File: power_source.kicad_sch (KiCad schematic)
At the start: 16 parts, among them CN1 KF250-3.5-2P-2, Q1 PJM2309PSC, U1 AP63203WU, U2 B0303S-1W_C883455

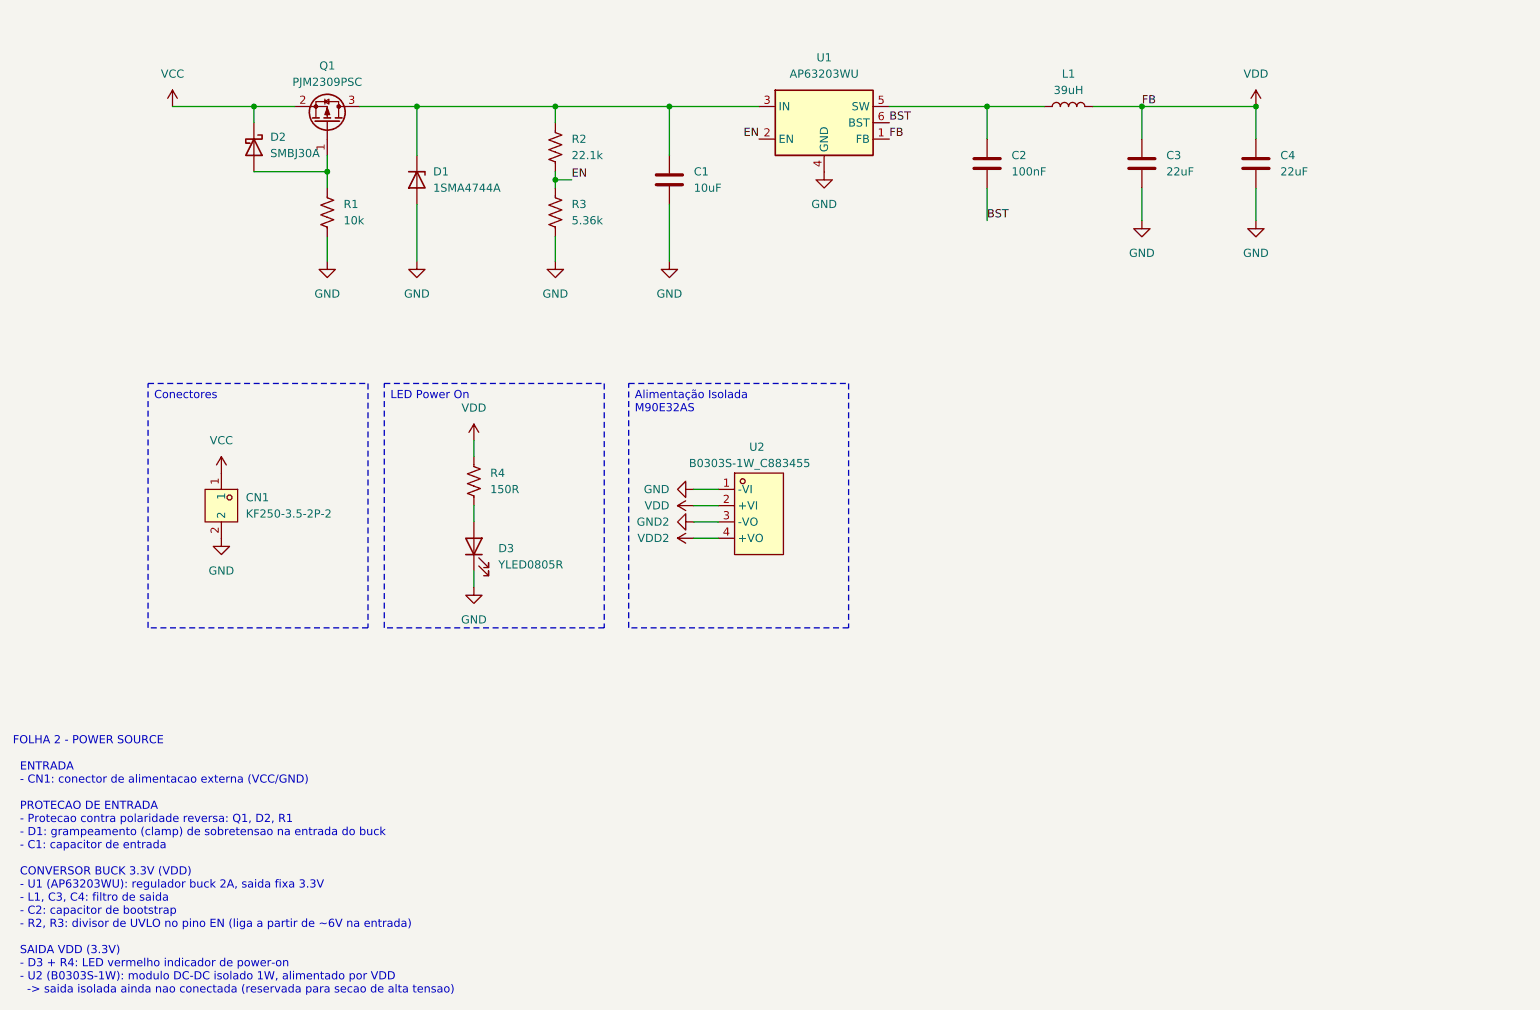
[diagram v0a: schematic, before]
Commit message: Checkpoint: MCU/M90E32AS/power_source rework, PCB layout, new sheets, library imports
- Rework mcu.kicad_sch, m90e32as.kicad_sch and power_source.kicad_sch: PM0/PM1/
  IRQ0/IRQ1 isolation wiring for the M90E32AS, USB-C native USB wiring, and
  related connector updates.
- Add analog_io.kicad_sch and digital_io.kicad_sch hierarchical sheets.
- Update ra5_2022.kicad_pcb layout and ra5_2022.kicad_pro settings.
- Import several LCSC components into the project library (connectors,
  inductor, SOT/SOIC footprints, USB-C connectors, power module).
- Fix import_lcsc_component.sh to normalize the "LCSC Part" field name to
  "LCSC Part #" on imported footprints too (previously only on symbols).
- Ignore local .claude/ state (worktrees/session data) in .gitignore.

Co-Authored-By: Claude Sonnet 5 <noreply@anthropic.com>
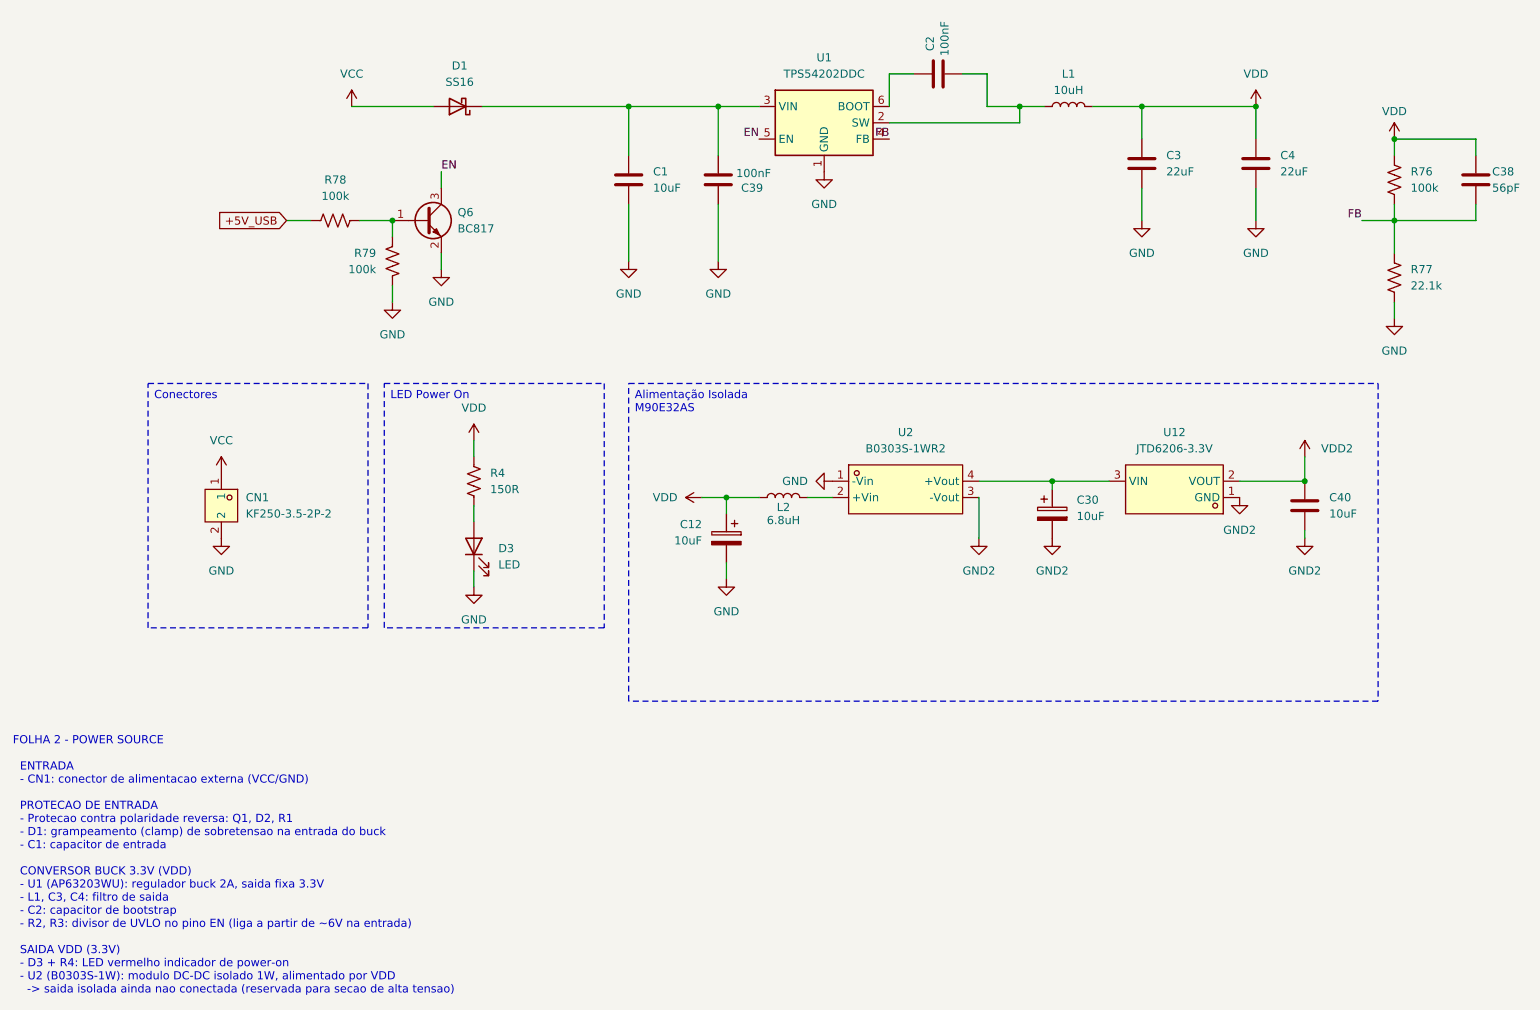
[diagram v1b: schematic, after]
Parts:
- removed D1: 1SMA4744A, Diode_SMD:D_SMA, symbol Device:D_Zener
- removed D2: SMBJ30A, Diode_SMD:D_SMB, symbol Device:D_Schottky
- removed Q1: PJM2309PSC, Package_TO_SOT_SMD:SOT-23, symbol Transistor_FET:Q_PMOS_GSD
- removed R1: 10k, Resistor_SMD:R_1206_3216Metric, symbol Device:R_US
- removed R2: 22.1k, Resistor_SMD:R_0603_1608Metric, symbol Device:R_US
- removed R3: 5.36k, Resistor_SMD:R_0603_1608Metric, symbol Device:R_US
- removed U1: AP63203WU, Package_TO_SOT_SMD:TSOT-23-6, symbol Regulator_Switching:AP63203WU
- removed U2: B0303S-1W_C883455, ra5_2022:PWRM-TH_B2415S-1W, symbol ra5_2022:B0303S-1W_C883455
- added C12, C30: 10uF, Capacitor_SMD:CP_Elec_4x5.4, symbol Device:C_Polarized
- added C38: 56pF, Capacitor_SMD:C_0402_1005Metric, symbol Device:C
- added C39: 100nF, Capacitor_SMD:C_0402_1005Metric, symbol Device:C
- added C40: 10uF, Capacitor_SMD:C_0603_1608Metric, symbol Device:C
- added D1: SS16, Diode_SMD:D_SMA, symbol Device:D_Schottky
- added L2: 6.8uH, Inductor_SMD:L_1008_2520Metric, symbol Device:L
- added Q6: BC817, Package_TO_SOT_SMD:SOT-23, symbol Transistor_BJT:BC817
- added R76, R78, R79: 100k, Resistor_SMD:R_0402_1005Metric, symbol Device:R_US
- added R77: 22.1k, Resistor_SMD:R_0402_1005Metric, symbol Device:R_US
- added U1: TPS54202DDC, Package_TO_SOT_SMD:SOT-23-6, symbol Regulator_Switching:TPS54202DDC
- added U12: JTD6206-3.3V, ra5_2022:SOT-23-3_L3.0-W1.7-P0.95-LS2.9-BR, symbol ra5_2022:JTD6206-3.3V
- added U2: B0303S-1WR2, ra5_2022:PWRM-TH_BXXXXS-1WR2, symbol ra5_2022:B0303S-1WR2_C7598619-1
- C2: footprint Capacitor_SMD:C_0603_1608Metric -> Capacitor_SMD:C_0201_0603Metric; LCSC Part # C48579280 -> C7393837; MPN 0603X7R104K250NT -> TCC0201X7R104K100ZT
- C3, C4: footprint Capacitor_SMD:C_0402_1005Metric -> Capacitor_SMD:C_1210_3225Metric; LCSC Part # C6119784 -> C309062; MPN CGA0402X5R226M6R3GT -> CL32B226KAJNNNE
- CN1: LCSC Part # (none) -> C475163
- D3: value YLED0805R -> LED; LCSC Part # (none) -> C19171391; MPN (none) -> YLED0805R
- L1: value 39uH -> 10uH; footprint Inductor_SMD:L_0603_1608Metric -> ra5_2022:IND-SMD_L7.0-W6.6; LCSC Part # C50325714 -> C5307622; MPN APLD1608-3R9KPTD3 -> XR0630-100M
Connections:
- net BST is gone; now on an unnamed net: C2.2
- net EN: now also Q6.3 (C), U1.5 (EN)
- net GND: now also C12.2, C39.1, Q6.2 (E), R77.2, R79.2, U1.1 (GND), U2.1 (-Vin)
- net GND2: now also C30.2, C40.2, U12.1 (GND), U2.3 (-Vout)
- net VCC: now also D1.2 (A)
- net VDD: now also C12.1, C38.1, L2.1, R76.1
- net VDD2: now also C40.1, U12.2 (VOUT)
- net at L1.1: now also U1.2 (SW); no longer C2.1
- net at C1.1: now also C39.2, D1.1 (K), U1.3 (VIN)
- new net: Q6.1 (B), R78.2, R79.1
- new net: C2.1, U1.6 (BOOT)
- new net: L2.2, U2.2 (+Vin)
- new net: C30.1, U12.3 (VIN), U2.4 (+Vout)
- new net +5V_USB: R78.1
- new net FB: C38.2, R76.2, R77.1, U1.4 (FB)
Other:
- moved on the sheet: C1, C2

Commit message: Checkpoint: RA5 base board finished, M.2 shield interconnect defined
Base board (ra5_2022):
- Finalize component placement on ra5_2022.kicad_pcb; next step is routing
- Add STM8S003F3P to bridge the 2 digital inputs / 2 digital outputs onto
  the shared I2C bus (alongside the ADS1115), freeing up M.2 pins
- Wire J1 (M.2 Key-E) to a custom, non-spec-compliant 3.3V pinout: I2C
  (SDA/SCL/ALERT#) on the native pins, M90E32AS SPI reusing the SD/SDIO
  "SPI mode" pin convention (SCLK/MOSI/MISO/CS), PM0/PM1 on VENDOR_DEFINED
  pins, USB-C passthrough, full GND/VDD
- Fix AS0BC21-S40BE-7H footprint: pads 76/77 (shield/ground tabs, not part
  of the 75-pin M.2 spec) remapped onto the GND pin instead of dangling
- Swap the buck inductor (L2) for SLW5040S100MST (C182189): same 10uH,
  lower DCR, 5x5mm footprint to clear a routing constraint
- Remove the unused "Production" KiCad Design Variant and align the
  remaining "Develop" variant's footprints with the defaults -- a
  variant/default footprint mismatch was causing Update PCB from Schematic
  to silently duplicate footprints on every sync
- Clean up 10 further orphaned duplicate footprints left on the PCB from
  earlier design revisions (R11, R12, C14, C16, C17, C18, C29, C31, C32, C35)
- Fix 3D model paths across the shared library to use the RA5_2022_LIB
  environment variable instead of ${KIPRJMOD}, so previews resolve
  correctly from sibling projects too

New sibling project (ra5_shield_modem/):
- MCU + LTE modem card, built to the M.2 Key-E mechanical form factor to
  plug into the base board's J1
- Share the ra5_2022 parts library via sym-lib-table/fp-lib-table
- Add the timonsku/M.2-Card-Footprints submodule as a card-edge template

Co-Authored-By: Claude Sonnet 5 <noreply@anthropic.com>
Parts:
- L2: renamed from L1; footprint ra5_2022:IND-SMD_L7.0-W6.6 -> ra5_2022:IND-SMD_L5.0-W5.0-1; LCSC Part # C5307622 -> C182189; MPN XR0630-100M -> SLW5040S100MST
- renumbered C39 to C2, C12 to C3, C2 to C4, C30 to C5, C3 to C6, C4 to C7, C40 to C8, C38 to C9, D3 to D2, L2 to L1, Q6 to Q1, R78 to R1, R79 to R2, R4 to R3, R76 to R4, R77 to R5, U1 to U2, U2 to U3, U12 to U4

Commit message: Migra componentes das bibliotecas LCSC locais para pecas JLCPCB
Troca os part numbers para casar com o estoque da JLCPCB e com o
catalogo PCBA Basic, eliminando a biblioteca local que era importada
via easyeda2kicad.

- Remove libraries/ (simbolos, footprints e modelos 3D importados) e o
  script import_lcsc_component.sh
- Adiciona o plugin JLCPCB (jlcpcb/project.db) e os scripts auxiliares
  fix_jlcpcb_tools_deps.sh e generate_ibom.sh
- Atualiza as cinco folhas do esquematico, o PCB e as regras de projeto

O PCB fica em estado intermediario: os componentes novos ainda precisam
ser reposicionados e as trilhas refeitas.

Co-Authored-By: Claude Opus 5 (1M context) <noreply@anthropic.com>
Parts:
- removed C3: 10uF, Capacitor_SMD:CP_Elec_4x5.4, symbol Device:C_Polarized
- added C41: 10uF, Capacitor_SMD:CP_Elec_4x5.4, symbol Device:C_Polarized
- C1: footprint Capacitor_SMD:C_0603_1608Metric -> Capacitor_SMD:C_1206_3216Metric; JLCPCB Part # (none) -> C13585; LCSC Part # C22367826 -> (none); MPN HGC0603R5106K350NTHJ -> CL31A106KBHNNNE
- C2: JLCPCB Part # (none) -> C307331; LCSC Part # C5448791 -> (none); MPN TCC0402X7R104K500AT -> CL05B104KB54PNC
- C4: footprint Capacitor_SMD:C_0201_0603Metric -> Capacitor_SMD:C_0402_1005Metric; JLCPCB Part # (none) -> C1525; LCSC Part # C7393837 -> (none); MPN TCC0201X7R104K100ZT -> CL05B104KO5NNNC
- C5: JLCPCB Part # (none) -> C22383768; LCSC Part # C3001198 -> (none); MPN CS1C100M-CRC54 -> VT1E100M0405
- C6, C7: footprint Capacitor_SMD:C_1210_3225Metric -> Capacitor_SMD:C_0603_1608Metric; JLCPCB Part # (none) -> C59461; LCSC Part # C309062 -> (none); MPN CL32B226KAJNNNE -> CL10A226MQ8NRNC
- C8: footprint Capacitor_SMD:C_0603_1608Metric -> Capacitor_SMD:C_0402_1005Metric; JLCPCB Part # (none) -> C15525; LCSC Part # C22367826 -> (none); MPN HGC0603R5106K350NTHJ -> CL05A106MQ5NUNC
- C9: footprint Capacitor_SMD:C_0402_1005Metric -> Capacitor_SMD:C_0603_1608Metric; JLCPCB Part # (none) -> C39148; LCSC Part # C7393845 -> (none); MPN TCC0402COG560K500AT -> CL10C560JB8NNNC
- CN1: JLCPCB Part # (none) -> C475163; LCSC Part C475163 -> (none); LCSC Part # C475163 -> (none)
- D1: value SS16 -> SS210; JLCPCB Part # (none) -> C14996; LCSC Part # C3035969 -> (none); MPN SS16 -> SS210
- D2: JLCPCB Part # (none) -> C19171391; LCSC Part # C19171391 -> (none)
- L1: JLCPCB Part # (none) -> C48533097; LCSC Part # C48533097 -> (none)
- L2: JLCPCB Part # (none) -> C182189; LCSC Part # C182189 -> (none)
- Q1: value BC817 -> BC817-25; JLCPCB Part # (none) -> C20069154; LCSC Part # C549433 -> (none); MPN BC817-25,235 -> BC817-25
- R1, R2, R4: footprint Resistor_SMD:R_0402_1005Metric -> Resistor_SMD:R_0805_2012Metric; JLCPCB Part # (none) -> C149504; LCSC Part # C54531015 -> (none); MPN 1RC0402J0104 -> 0805W8F1003T5E
- R3: JLCPCB Part # (none) -> C22808; LCSC Part # C54920974 -> (none); MPN HRC0603J151 ENTN -> 0603WAF1500T5E
- R5: value 22.1k -> 22k; JLCPCB Part # (none) -> C25768; LCSC Part # C54530781 -> (none); MPN 1RC0402F2212 -> 0402WGF2202TCE
- U2: JLCPCB Part # (none) -> C191884; LCSC Part # C191884 -> (none)
- U3: JLCPCB Part # (none) -> C7598619; LCSC Part # C7598619 -> (none)
- U4: value JTD6206-3.3V -> XC6206P332MR-JSM; JLCPCB Part # (none) -> C20616640; LCSC Part # C42443428 -> (none); MPN JTD6206-3.3V -> XC6206P332MR-JSM; Manufacturer JTD(晶泰达) -> (none)
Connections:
- net FB: now also R4.1; no longer R4.2
- net GND: now also R2.1, C41.2; no longer R2.2
- net VDD: now also R4.2, C41.1; no longer R4.1
- net at Q1.1 (B), R1.2: now also R2.2; no longer R2.1

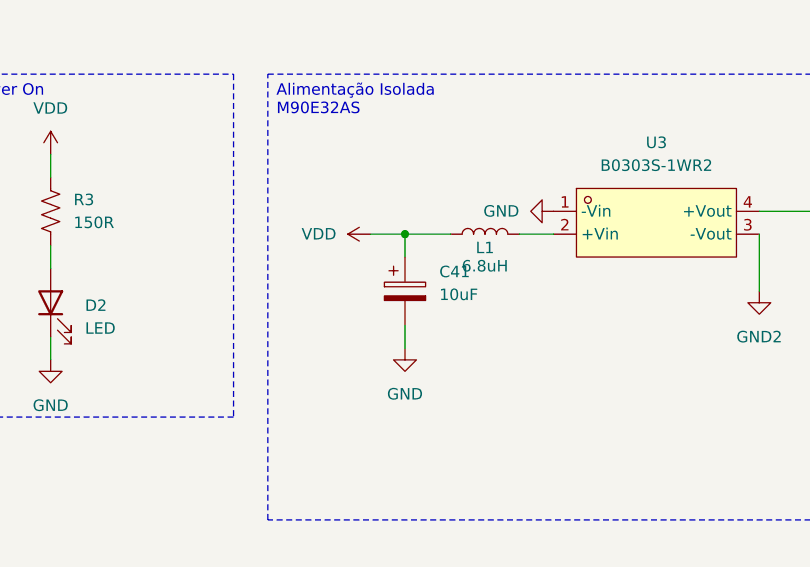
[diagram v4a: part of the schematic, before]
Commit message: Reintroduz biblioteca local ra5_2022 e atualiza layout/esquematicos
Volta a usar simbolos, footprints e modelos 3D importados via
easyeda2kicad (libraries/) em vez das pecas basicas JLCPCB adotadas no
commit anterior, alem de atualizar o roteamento/posicionamento no PCB
e as cinco folhas do esquematico.

Co-Authored-By: Claude Sonnet 5 <noreply@anthropic.com>
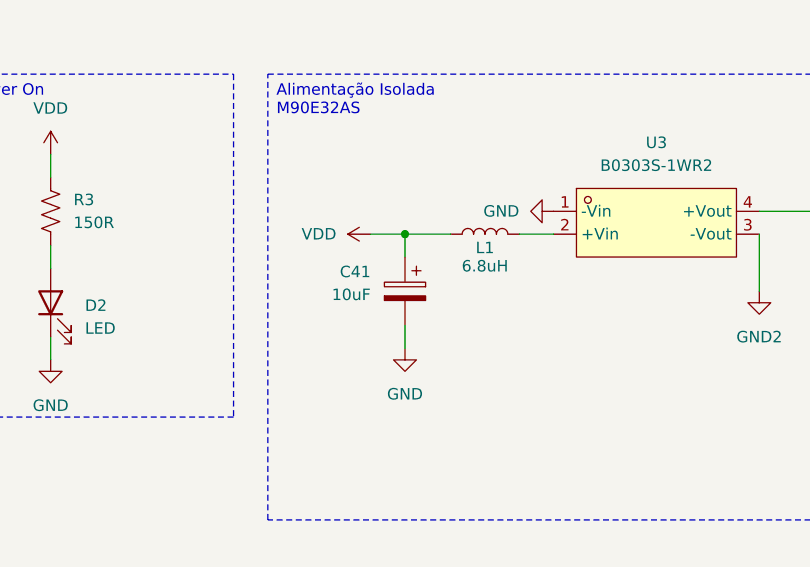
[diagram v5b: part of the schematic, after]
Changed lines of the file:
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@@
 		(lib_id "Device:C_Polarized")
 		(at 137.16 113.03 0)
+		(mirror y)
 		(unit 1)
 		(body_style 1)
@@
 		(dnp no)
 		(property "Reference" "C41"
-			(at 140.97 110.8709 0)
+			(at 133.35 110.8709 0)
 			(show_name no)
 			(do_not_autoplace no)
@@
 		)
 		(property "Value" "10uF"
-			(at 140.97 113.4109 0)
+			(at 133.35 113.4109 0)
 			(show_name no)
 			(do_not_autoplace no)
@@
 		)
 		(property "Footprint" "Capacitor_SMD:CP_Elec_4x5.4"
-			(at 138.1252 116.84 0)
+			(at 136.1948 116.84 0)
 			(hide yes)
 			(show_name no)
@@
 						(field
 							(name "Footprint")
-							(value "Capacitor_SMD:C_1210_3225Metric")
+							(value "Capacitor_SMD:C_0603_1608Metric")
 						)
 						(field
@@
 			)
 		)
-		(property "LCSC Part" ""
-			(at 201.93 54.61 0)
-			(hide yes)
-			(show_name no)
-			(do_not_autoplace no)
-			(effects
-				(font
-					(size 1.27 1.27)
-				)
-			)
-		)
-		(property "KLC_S3.3" ""
-			(at 201.93 54.61 0)
-			(hide yes)
-			(show_name no)
-			(do_not_autoplace no)
-			(effects
-				(font
-					(size 1.27 1.27)
-				)
-			)
-		)
-		(property "KLC_S4.1" ""
-			(at 201.93 54.61 0)
-			(hide yes)
-			(show_name no)
-			(do_not_autoplace no)
-			(effects
-				(font
-					(size 1.27 1.27)
-				)
-			)
-		)
-		(property "LCSC Part #" ""
-			(at 201.93 54.61 0)
-			(hide yes)
-			(show_name no)
-			(do_not_autoplace no)
-			(effects
-				(font
-					(size 1.27 1.27)
-				)
-			)
-		)
 		(pin "1"
 		)
@@
 						(field
 							(name "Footprint")
-							(value "Capacitor_SMD:C_1210_3225Metric")
+							(value "Capacitor_SMD:C_0603_1608Metric")
 						)
 						(field
